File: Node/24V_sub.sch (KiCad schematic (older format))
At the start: 20 parts, among them U401 TPS54361

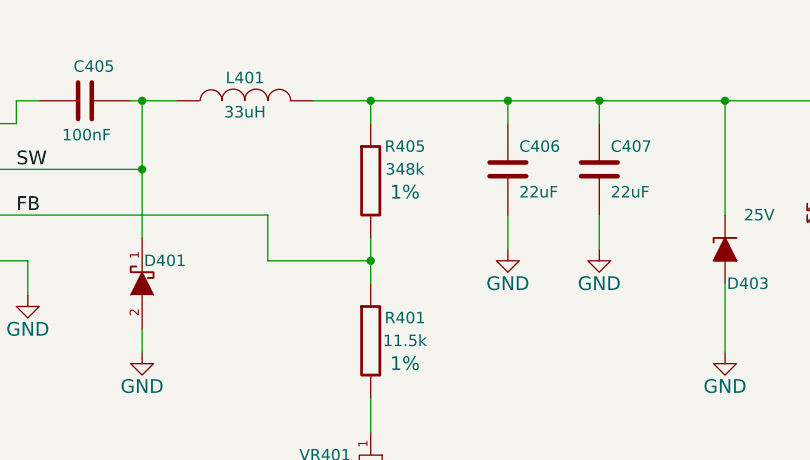
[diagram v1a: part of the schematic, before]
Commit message: Generated BOM, filled out part numbers for precision resistors and headers.
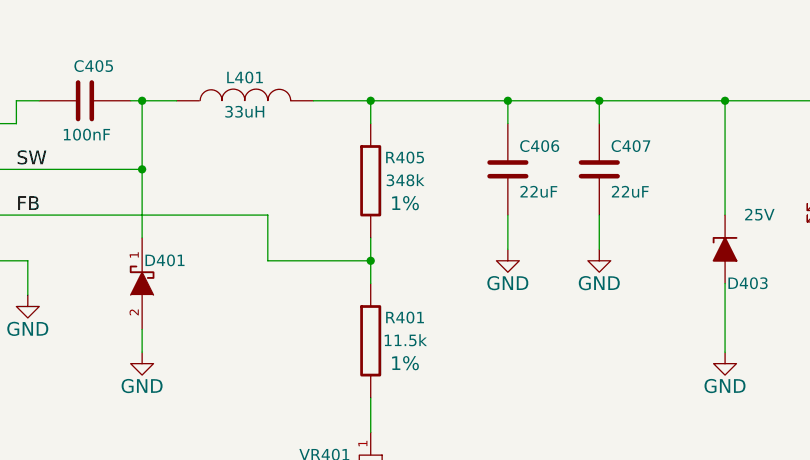
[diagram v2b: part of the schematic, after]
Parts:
- R401: MFG. P/N (none) -> RC0805FR-0711K5L; Manufacturer (none) -> Yageo; Vendor (none) -> DigiKey; Vendor P/N (none) -> 311-11.5KCRCT-ND
- R405: MFG. P/N (none) -> RC0805FR-07348KL; Manufacturer (none) -> Yageo; Mfg. Name Yageo -> (none); Mfg. Part Num RC0805FR-07348KL -> (none); Vendor (none) -> DigiKey; Vendor P/N (none) -> 311-348KCRCT-ND; Vendor Part Num 311-348KCRCT-ND -> (none)
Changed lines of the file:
@@
 EESchema Schematic File Version 2
 LIBS:hyper_capstone
+LIBS:Connector
 LIBS:node-cache
 EELAYER 25 0
@@
 	3150 2700 3150 2900
 $Comp
-L GND #PWR409
+L GND #PWR022
 U 1 1 59DF0C8F
 P 3150 2900
-F 0 "#PWR409" H 3150 2650 60  0001 C CNN
+F 0 "#PWR022" H 3150 2650 60  0001 C CNN
 F 1 "GND" H 3150 2750 60  0000 C CNN
 F 2 "" H 3150 2900 60  0000 C CNN
@@
 	2650 2550 2650 2900
 $Comp
-L GND #PWR408
+L GND #PWR023
 U 1 1 59DF0CDB
 P 2650 2900
-F 0 "#PWR408" H 2650 2650 60  0001 C CNN
+F 0 "#PWR023" H 2650 2650 60  0001 C CNN
 F 1 "GND" H 2650 2750 60  0000 C CNN
 F 2 "" H 2650 2900 60  0000 C CNN
@@
 Connection ~ 3600 3800
 $Comp
-L GND #PWR412
+L GND #PWR024
 U 1 1 59DF0D79
 P 3600 3850
-F 0 "#PWR412" H 3600 3600 60  0001 C CNN
+F 0 "#PWR024" H 3600 3600 60  0001 C CNN
 F 1 "GND" H 3600 3700 60  0000 C CNN
 F 2 "" H 3600 3850 60  0000 C CNN
@@
 	5550 2350 5550 2500
 $Comp
-L GND #PWR403
+L GND #PWR025
 U 1 1 59DF11FB
 P 5550 2500
-F 0 "#PWR403" H 5550 2250 60  0001 C CNN
+F 0 "#PWR025" H 5550 2250 60  0001 C CNN
 F 1 "GND" H 5550 2350 60  0000 C CNN
 F 2 "" H 5550 2500 60  0000 C CNN
@@
 	6050 2650 6050 2750
 $Comp
-L GND #PWR405
+L GND #PWR026
 U 1 1 59DF12E3
 P 6050 2750
-F 0 "#PWR405" H 6050 2500 60  0001 C CNN
+F 0 "#PWR026" H 6050 2500 60  0001 C CNN
 F 1 "GND" H 6050 2600 60  0000 C CNN
 F 2 "" H 6050 2750 60  0000 C CNN
@@
 $EndComp
 Connection ~ 6050 1650
-$Comp
-L R_large R405
-U 1 1 59DF140F
-P 7050 2000
-F 0 "R405" H 7200 2150 50  0000 C CNN
-F 1 "348k" H 7200 2050 50  0000 C CNN
-F 2 "Resistors_SMD:R_0805_HandSoldering" V 6980 2000 30  0001 C CNN
-F 3 "" H 7050 2000 30  0000 C CNN
-F 4 "RC0805FR-07348KL" H 7050 2000 60  0001 C CNN "Mfg. Part Num"
-F 5 "Yageo" H 7050 2000 60  0001 C CNN "Mfg. Name"
-F 6 "311-348KCRCT-ND" H 7050 2000 60  0001 C CNN "Vendor Part Num"
-F 7 "Digi-Key" H 7050 2000 60  0001 C CNN "Vendor Name"
-F 8 "1%" H 7200 1950 60  0000 C CNN "Tolerance"
-	1    7050 2000
-	1    0    0    -1
-$EndComp
 Wire Wire Line
 	5400 2150 6600 2150
@@
 Connection ~ 7050 2350
 $Comp
-L GND #PWR411
+L GND #PWR027
 U 1 1 59DF1632
 P 7050 3700
-F 0 "#PWR411" H 7050 3450 60  0001 C CNN
+F 0 "#PWR027" H 7050 3450 60  0001 C CNN
 F 1 "GND" H 7050 3550 60  0000 C CNN
 F 2 "" H 7050 3700 60  0000 C CNN
@@
 	7650 2150 7650 2300
 $Comp
-L GND #PWR401
+L GND #PWR028
 U 1 1 59DF19E0
 P 7650 2300
-F 0 "#PWR401" H 7650 2050 60  0001 C CNN
+F 0 "#PWR028" H 7650 2050 60  0001 C CNN
 F 1 "GND" H 7650 2150 60  0000 C CNN
 F 2 "" H 7650 2300 60  0000 C CNN
@@
 	4700 2650 4700 2750
 $Comp
-L GND #PWR404
+L GND #PWR029
 U 1 1 59F17967
 P 4700 2750
-F 0 "#PWR404" H 4700 2500 60  0001 C CNN
+F 0 "#PWR029" H 4700 2500 60  0001 C CNN
 F 1 "GND" H 4700 2600 60  0000 C CNN
 F 2 "" H 4700 2750 60  0000 C CNN
@@
 	2050 2100 2050 2850
 $Comp
-L GND #PWR407
+L GND #PWR030
 U 1 1 59F1943C
 P 2050 2850
-F 0 "#PWR407" H 2050 2600 60  0001 C CNN
+F 0 "#PWR030" H 2050 2600 60  0001 C CNN
 F 1 "GND" H 2050 2700 60  0000 C CNN
 F 2 "" H 2050 2850 60  0000 C CNN
@@
 	8050 2150 8050 2300
 $Comp
-L GND #PWR402
+L GND #PWR031
 U 1 1 59F197CD
 P 8050 2300
-F 0 "#PWR402" H 8050 2050 60  0001 C CNN
+F 0 "#PWR031" H 8050 2050 60  0001 C CNN
 F 1 "GND" H 8050 2150 60  0000 C CNN
 F 2 "" H 8050 2300 60  0000 C CNN
@@
 	8600 2450 8600 2750
 $Comp
-L GND #PWR406
+L GND #PWR032
 U 1 1 59F1A7A5
 P 8600 2750
-F 0 "#PWR406" H 8600 2500 60  0001 C CNN
+F 0 "#PWR032" H 8600 2500 60  0001 C CNN
 F 1 "GND" H 8600 2600 60  0000 C CNN
 F 2 "" H 8600 2750 60  0000 C CNN
@@
 	9050 3250 9050 3400
 $Comp
-L GND #PWR410
+L GND #PWR033
 U 1 1 59F1AA93
 P 9050 3400
-F 0 "#PWR410" H 9050 3150 60  0001 C CNN
+F 0 "#PWR033" H 9050 3150 60  0001 C CNN
 F 1 "GND" H 9050 3250 60  0000 C CNN
 F 2 "" H 9050 3400 60  0000 C CNN
@@
 F 2 "Resistors_SMD:R_0805_HandSoldering" V 6980 2700 30  0001 C CNN
 F 3 "" H 7050 2700 30  0000 C CNN
-F 4 "Digi-Key" H 7050 2700 60  0001 C CNN "Vendor Name"
-F 5 "1%" H 7200 2600 60  0000 C CNN "Tolerance"
+F 4 "Yageo" H 7050 2700 60  0001 C CNN "Manufacturer"
+F 5 "RC0805FR-0711K5L" H 7050 2700 60  0001 C CNN "MFG. P/N"
+F 6 "DigiKey" H 7050 2700 60  0001 C CNN "Vendor"
+F 7 "311-11.5KCRCT-ND" H 7050 2700 60  0001 C CNN "Vendor P/N"
+F 8 "1%" H 7200 2600 60  0000 C CNN "Tolerance"
+F 9 "Digi-Key" H 7050 2700 60  0001 C CNN "Vendor Name"
 	1    7050 2700
 	1    0    0    -1
@@
 Wire Wire Line
 	7050 2950 7050 3100
+$Comp
+L R_large R405
+U 1 1 5A72026D
+P 7050 2000
+F 0 "R405" H 7200 2100 50  0000 C CNN
+F 1 "348k" H 7200 2000 50  0000 C CNN
+F 2 "Resistors_SMD:R_0805_HandSoldering" V 6980 2000 30  0001 C CNN
+F 3 "" H 7050 2000 30  0000 C CNN
+F 4 "Yageo" H 7050 2000 60  0001 C CNN "Manufacturer"
+F 5 "RC0805FR-07348KL" H 7050 2000 60  0001 C CNN "MFG. P/N"
+F 6 "DigiKey" H 7050 2000 60  0001 C CNN "Vendor"
+F 7 "311-348KCRCT-ND" H 7050 2000 60  0001 C CNN "Vendor P/N"
+F 8 "1%" H 7200 1900 60  0000 C CNN "Tolerance"
+F 9 "Digi-Key" H 7050 2000 60  0001 C CNN "Vendor Name"
+	1    7050 2000
+	1    0    0    -1
+$EndComp
 $EndSCHEMATC

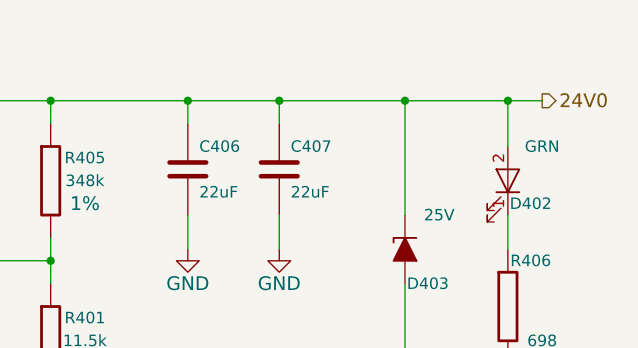
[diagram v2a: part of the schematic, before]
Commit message: Added testpoints and silkscreen descriptions to PCB. Added Paradigm template to schematic.
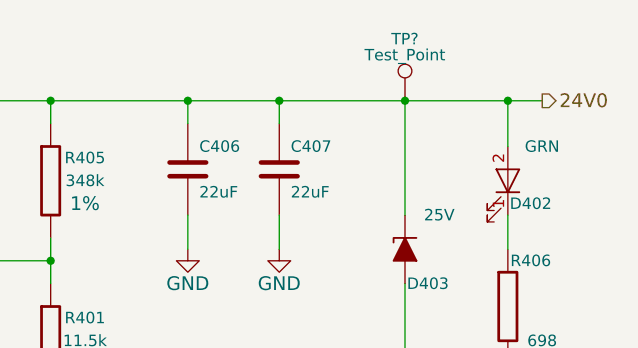
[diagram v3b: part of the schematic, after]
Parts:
- added TP?: Test_Point, Measurement_Points:Test_Point_Keystone_5000-5004_Miniature, symbol Test_Point
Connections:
- net 24V0: now also TP?.1
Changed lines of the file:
@@
 encoding utf-8
 Sheet 4 22
-Title ""
+Title "Node Board"
 Date ""
-Rev ""
+Rev "Rev 1.0"
 Comp ""
 Comment1 ""
@@
 	1    0    0    -1
 $EndComp
+$Comp
+L Test_Point TP?
+U 1 1 5A71F218
+P 8600 1650
+F 0 "TP?" H 8600 1920 50  0000 C CNN
+F 1 "Test_Point" H 8600 1850 50  0000 C CNN
+F 2 "Measurement_Points:Test_Point_Keystone_5000-5004_Miniature" H 8800 1650 50  0001 C CNN
+F 3 "" H 8800 1650 50  0001 C CNN
+F 4 "Keystone Electronics" H 8600 1650 60  0001 C CNN "Manufacturer"
+F 5 "5000" H 8600 1650 60  0001 C CNN "Manufacturer P/N"
+F 6 "DigiKey" H 8600 1650 60  0001 C CNN "Vendor"
+F 7 "36-5000-ND" H 8600 1650 60  0001 C CNN "Vendor P/N"
+	1    8600 1650
+	1    0    0    -1
+$EndComp

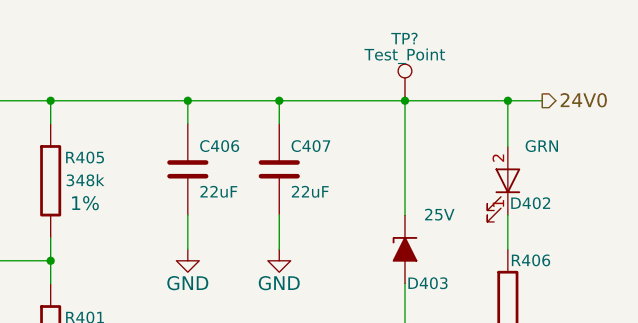
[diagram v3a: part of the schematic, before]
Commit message: fixed and routed driver spi issue
Added new rx/tx bus for solenoid driver. Routed it too. Nice.
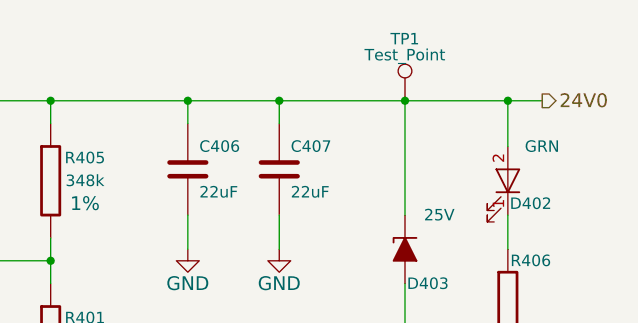
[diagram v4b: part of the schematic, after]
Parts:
- gave numbers to parts that had none: 1
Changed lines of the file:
@@
 EESchema Schematic File Version 2
 LIBS:hyper_capstone
-LIBS:Connector
 LIBS:node-cache
 EELAYER 25 0
@@
 $EndComp
 $Comp
-L Test_Point TP?
+L Test_Point TP1
 U 1 1 5A71F218
 P 8600 1650
-F 0 "TP?" H 8600 1920 50  0000 C CNN
+F 0 "TP1" H 8600 1920 50  0000 C CNN
 F 1 "Test_Point" H 8600 1850 50  0000 C CNN
 F 2 "Measurement_Points:Test_Point_Keystone_5000-5004_Miniature" H 8800 1650 50  0001 C CNN

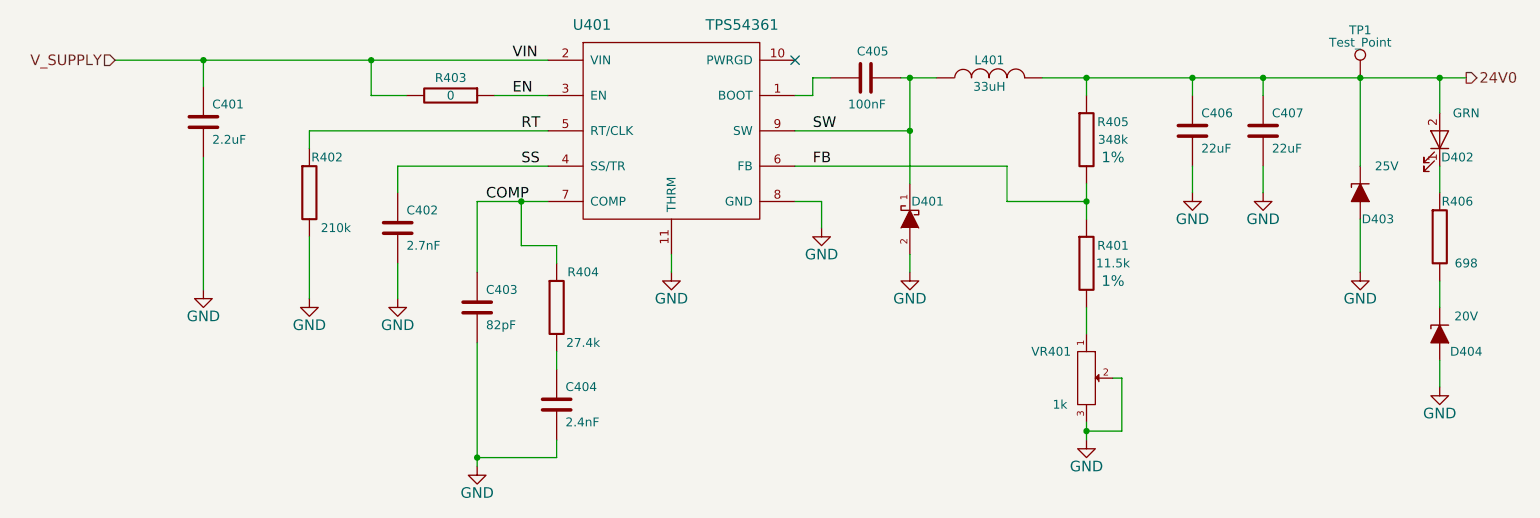
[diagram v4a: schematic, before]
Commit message: Updated bom stuff, made new gerbers and added a trace route
damn,
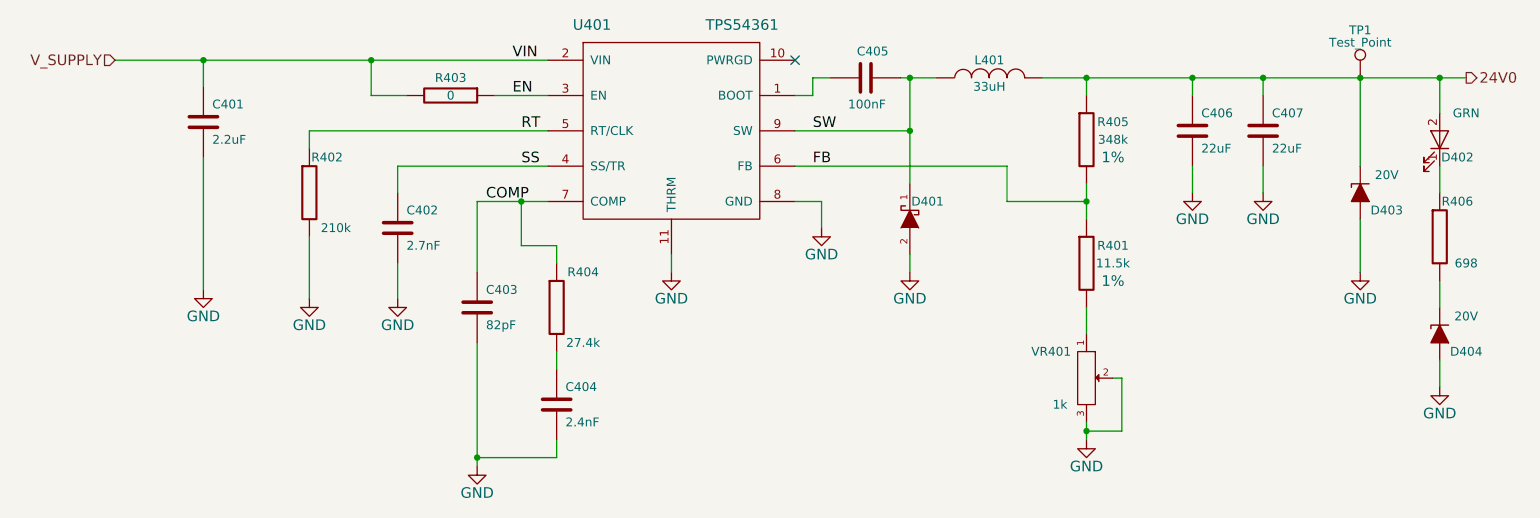
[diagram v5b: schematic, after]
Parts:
- D403: value 25V -> 20V; footprint Diodes_SMD:D_SOD-123 -> Diodes_SMD:D_SOD-323_HandSoldering; Mfg. Part Num MMSZ4710T1G -> MM3Z20VT1G; Vendor Name Digi-Key -> (none); Vendor Part Num MMSZ4710T1GOSCT-ND -> MM3Z20VST1GOSCT-ND
- D404: Vendor Part Num MM3Z20VT1GOSCT-ND -> MM3Z20VST1GOSCT-ND
- R402: Mfg. Name Yageo -> Panasonic Electronic Components; Mfg. Part Num RC0805FR-07210KL -> ERA-6AEB2103V; Vendor Part Num 311-210KCRCT-ND -> P210KDACT-ND
- R403: Mfg. Name Yageo -> Panasonic Electronic Components; Mfg. Part Num RC0805JR-070RL -> ERJ-6GEY0R00V; Vendor Part Num 311-0.0ARCT-ND -> P0.0ACT-ND
- VR401: Vendor Part Num 490-2881-ND -> (none)
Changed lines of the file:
@@
 F 2 "Resistors_SMD:R_0805_HandSoldering" V 3380 1750 30  0001 C CNN
 F 3 "" H 3450 1750 30  0000 C CNN
-F 4 "RC0805JR-070RL" H 3450 1750 60  0001 C CNN "Mfg. Part Num"
-F 5 "Yageo" H 3450 1750 60  0001 C CNN "Mfg. Name"
-F 6 "311-0.0ARCT-ND" H 3450 1750 60  0001 C CNN "Vendor Part Num"
+F 4 "ERJ-6GEY0R00V" H 3450 1750 60  0001 C CNN "Mfg. Part Num"
+F 5 "Panasonic Electronic Components" H 3450 1750 60  0001 C CNN "Mfg. Name"
+F 6 "P0.0ACT-ND" H 3450 1750 60  0001 C CNN "Vendor Part Num"
 F 7 "Digi-Key" H 3450 1750 60  0001 C CNN "Vendor Name"
 	1    3450 1750
@@
 F 2 "Resistors_SMD:R_0805_HandSoldering" V 2580 2300 30  0001 C CNN
 F 3 "" H 2650 2300 30  0000 C CNN
-F 4 "RC0805FR-07210KL" H 2650 2300 60  0001 C CNN "Mfg. Part Num"
-F 5 "Yageo" H 2650 2300 60  0001 C CNN "Mfg. Name"
-F 6 "311-210KCRCT-ND" H 2650 2300 60  0001 C CNN "Vendor Part Num"
+F 4 "ERA-6AEB2103V" H 2650 2300 60  0001 C CNN "Mfg. Part Num"
+F 5 "Panasonic Electronic Components" H 2650 2300 60  0001 C CNN "Mfg. Name"
+F 6 "P210KDACT-ND" H 2650 2300 60  0001 C CNN "Vendor Part Num"
 F 7 "Digi-Key" H 2650 2300 60  0001 C CNN "Vendor Name"
 	1    2650 2300
@@
 $EndComp
 Wire Wire Line
-	4000 2350 3600 2350
+	3600 2350 4000 2350
 Wire Wire Line
 	3600 2350 3600 2750
@@
 F 4 "23BR1KLFTR" H 7050 3350 60  0001 C CNN "Mfg. Part Num"
 F 5 "987-1015-1-ND" H 7050 3350 60  0001 C CNN "Mfg. Name"
-F 6 "490-2881-ND" H 7050 3350 60  0001 C CNN "Vendor Part Num"
-F 7 "Digi-Key" H 7050 3350 60  0001 C CNN "Vendor Name"
+F 6 "Digi-Key" H 7050 3350 60  0001 C CNN "Vendor Name"
 	1    7050 3350
 	0    1    1    0
@@
 	1    8050 1950
 	1    0    0    -1
-$EndComp
-$Comp
-L D_Zener_ALT D403
-U 1 1 59F1A0B3
-P 8600 2300
-F 0 "D403" V 8750 2200 50  0000 C CNN
-F 1 "25V" V 8450 2150 50  0000 C CNN
-F 2 "Diodes_SMD:D_SOD-123" H 8600 2300 60  0001 C CNN
-F 3 "" H 8600 2300 60  0000 C CNN
-F 4 "MMSZ4710T1G" H 8600 2300 60  0001 C CNN "Mfg. Part Num"
-F 5 "ON Semi" H 8600 2300 60  0001 C CNN "Mfg. Name"
-F 6 "MMSZ4710T1GOSCT-ND" H 8600 2300 60  0001 C CNN "Vendor Part Num"
-F 7 "Digi-Key" H 8600 2300 60  0001 C CNN "Vendor Name"
-	1    8600 2300
-	0    -1   1    0
 $EndComp
 $Comp
@@
 F 4 "MM3Z20VT1G" H 9050 3100 60  0001 C CNN "Mfg. Part Num"
 F 5 "ON Semi" H 9050 3100 60  0001 C CNN "Mfg. Name"
-F 6 "MM3Z20VT1GOSCT-ND" H 9050 3100 60  0001 C CNN "Vendor Part Num"
+F 6 "MM3Z20VST1GOSCT-ND" H 9050 3100 60  0001 C CNN "Vendor Part Num"
 	1    9050 3100
 	0    -1   1    0
@@
 	1    0    0    -1
 $EndComp
+$Comp
+L D_Zener_ALT D403
+U 1 1 5B52792D
+P 8600 2300
+F 0 "D403" V 8700 2150 50  0000 C CNN
+F 1 "20V" V 8500 2150 50  0000 C CNN
+F 2 "Diodes_SMD:D_SOD-323_HandSoldering" H 8600 2300 60  0001 C CNN
+F 3 "" H 8600 2300 60  0000 C CNN
+F 4 "MM3Z20VT1G" H 8600 2300 60  0001 C CNN "Mfg. Part Num"
+F 5 "ON Semi" H 8600 2300 60  0001 C CNN "Mfg. Name"
+F 6 "MM3Z20VST1GOSCT-ND" H 8600 2300 60  0001 C CNN "Vendor Part Num"
+	1    8600 2300
+	0    -1   1    0
+$EndComp
 $EndSCHEMATC

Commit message: Ghost train
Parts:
- C401, C402, C403, C404, C405, C406, C407: symbol C_large -> hyper_capstone:C_large
- D401: symbol DIODESCH -> node-rescue:DIODESCH
- D402: symbol LED -> node-rescue:LED
- D403, D404: symbol D_Zener_ALT -> node-rescue:D_Zener_ALT
- L401: symbol L_large -> hyper_capstone:L_large
- R401, R402, R403, R404, R405, R406: symbol R_large -> hyper_capstone:R_large
- TP1: symbol Test_Point -> node-rescue:Test_Point
- U401: symbol TPS54361 -> hyper_capstone:TPS54361
- VR401: symbol POT_large -> hyper_capstone:POT_large
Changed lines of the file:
@@
-EESchema Schematic File Version 2
-LIBS:hyper_capstone
+EESchema Schematic File Version 4
 LIBS:node-cache
-EELAYER 25 0
+EELAYER 26 0
 EELAYER END
 $Descr A4 11693 8268
@@
 V_SUPPLY
 $Comp
-L TPS54361 U401
+L hyper_capstone:TPS54361 U401
 U 1 1 59DF09C7
 P 4650 2000
@@
 	1550 1550 4000 1550
 $Comp
-L R_large R403
+L hyper_capstone:R_large R403
 U 1 1 59DF0A43
 P 3450 1750
@@
 	2650 1950 2650 2050
 $Comp
-L R_large R402
+L hyper_capstone:R_large R402
 U 1 1 59DF0ABF
 P 2650 2300
@@
 	3150 2150 3150 2300
 $Comp
-L C_large C402
+L hyper_capstone:C_large C402
 U 1 1 59DF0AF6
 P 3150 2500
@@
 	3600 2350 3600 2750
 $Comp
-L C_large C403
+L hyper_capstone:C_large C403
 U 1 1 59DF0B60
 P 3600 2950
@@
 $EndComp
 $Comp
-L R_large R404
+L hyper_capstone:R_large R404
 U 1 1 59DF0B8E
 P 4050 2950
@@
 $EndComp
 $Comp
-L C_large C404
+L hyper_capstone:C_large C404
 U 1 1 59DF0BD2
 P 4050 3500
@@
 	3150 2700 3150 2900
 $Comp
-L GND #PWR022
+L node-rescue:GND #PWR022
 U 1 1 59DF0C8F
 P 3150 2900
@@
 	2650 2550 2650 2900
 $Comp
-L GND #PWR023
+L node-rescue:GND #PWR023
 U 1 1 59DF0CDB
 P 2650 2900
@@
 Connection ~ 3600 3800
 $Comp
-L GND #PWR024
+L node-rescue:GND #PWR024
 U 1 1 59DF0D79
 P 3600 3850
@@
 $EndComp
 $Comp
-L C_large C405
+L hyper_capstone:C_large C405
 U 1 1 59DF0F63
 P 5800 1650
@@
 	6050 1650 6050 2250
 $Comp
-L L_large L401
+L hyper_capstone:L_large L401
 U 1 1 59DF110B
 P 6500 1650
@@
 $EndComp
 $Comp
-L DIODESCH D401
+L node-rescue:DIODESCH D401
 U 1 1 59DF1174
 P 6050 2450
@@
 	5550 2350 5550 2500
 $Comp
-L GND #PWR025
+L node-rescue:GND #PWR025
 U 1 1 59DF11FB
 P 5550 2500
@@
 	6050 2650 6050 2750
 $Comp
-L GND #PWR026
+L node-rescue:GND #PWR026
 U 1 1 59DF12E3
 P 6050 2750
@@
 Connection ~ 7050 2350
 $Comp
-L GND #PWR027
+L node-rescue:GND #PWR027
 U 1 1 59DF1632
 P 7050 3700
@@
 $EndComp
 $Comp
-L C_large C406
+L hyper_capstone:C_large C406
 U 1 1 59DF186C
 P 7650 1950
@@
 	7650 2150 7650 2300
 $Comp
-L GND #PWR028
+L node-rescue:GND #PWR028
 U 1 1 59DF19E0
 P 7650 2300
@@
 	4700 2650 4700 2750
 $Comp
-L GND #PWR029
+L node-rescue:GND #PWR029
 U 1 1 59F17967
 P 4700 2750
@@
 $EndComp
 $Comp
-L POT_large VR401
+L hyper_capstone:POT_large VR401
 U 1 1 59F16B09
 P 7050 3350
@@
 Connection ~ 7050 3650
 $Comp
-L C_large C401
+L hyper_capstone:C_large C401
 U 1 1 59F19207
 P 2050 1900
@@
 	2050 2100 2050 2850
 $Comp
-L GND #PWR030
+L node-rescue:GND #PWR030
 U 1 1 59F1943C
 P 2050 2850
@@
 	8050 2150 8050 2300
 $Comp
-L GND #PWR031
+L node-rescue:GND #PWR031
 U 1 1 59F197CD
 P 8050 2300
@@
 Connection ~ 8050 1650
 $Comp
-L C_large C407
+L hyper_capstone:C_large C407
 U 1 1 59F19D57
 P 8050 1950
@@
 $EndComp
 $Comp
-L LED D402
+L node-rescue:LED D402
 U 1 1 59F1A2D3
 P 9050 2000
@@
 $EndComp
 $Comp
-L R_large R406
+L hyper_capstone:R_large R406
 U 1 1 59F1A39A
 P 9050 2550
@@
 $EndComp
 $Comp
-L D_Zener_ALT D404
+L node-rescue:D_Zener_ALT D404
 U 1 1 59F1A3FC
 P 9050 3100
@@
 	8600 2450 8600 2750
 $Comp
-L GND #PWR032
+L node-rescue:GND #PWR032
 U 1 1 59F1A7A5
 P 8600 2750
@@
 	9050 3250 9050 3400
 $Comp
-L GND #PWR033
+L node-rescue:GND #PWR033
 U 1 1 59F1AA93
 P 9050 3400
@@
 FB
 $Comp
-L R_large R401
+L hyper_capstone:R_large R401
 U 1 1 5A10BB15
 P 7050 2700
@@
 	7050 2950 7050 3100
 $Comp
-L R_large R405
+L hyper_capstone:R_large R405
 U 1 1 5A72026D
 P 7050 2000
@@
 $EndComp
 $Comp
-L Test_Point TP1
+L node-rescue:Test_Point TP1
 U 1 1 5A71F218
 P 8600 1650
@@
 $EndComp
 $Comp
-L D_Zener_ALT D403
+L node-rescue:D_Zener_ALT D403
 U 1 1 5B52792D
 P 8600 2300
